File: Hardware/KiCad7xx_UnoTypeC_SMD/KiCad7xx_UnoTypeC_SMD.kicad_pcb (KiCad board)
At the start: 2 copper layers, 68.6 x 53.3 mm, 75 parts, among them J1 -, J2 -, T1 FDN340P, U1 NCP1117ST50T3G, U2 LP2985-33DBVR, U3 16U2, U4 ATMEGA328P-MU, U5 LMV358IDGKR, X1 POWERSUPPLY_DC21MMX, X2 USB-B_TH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

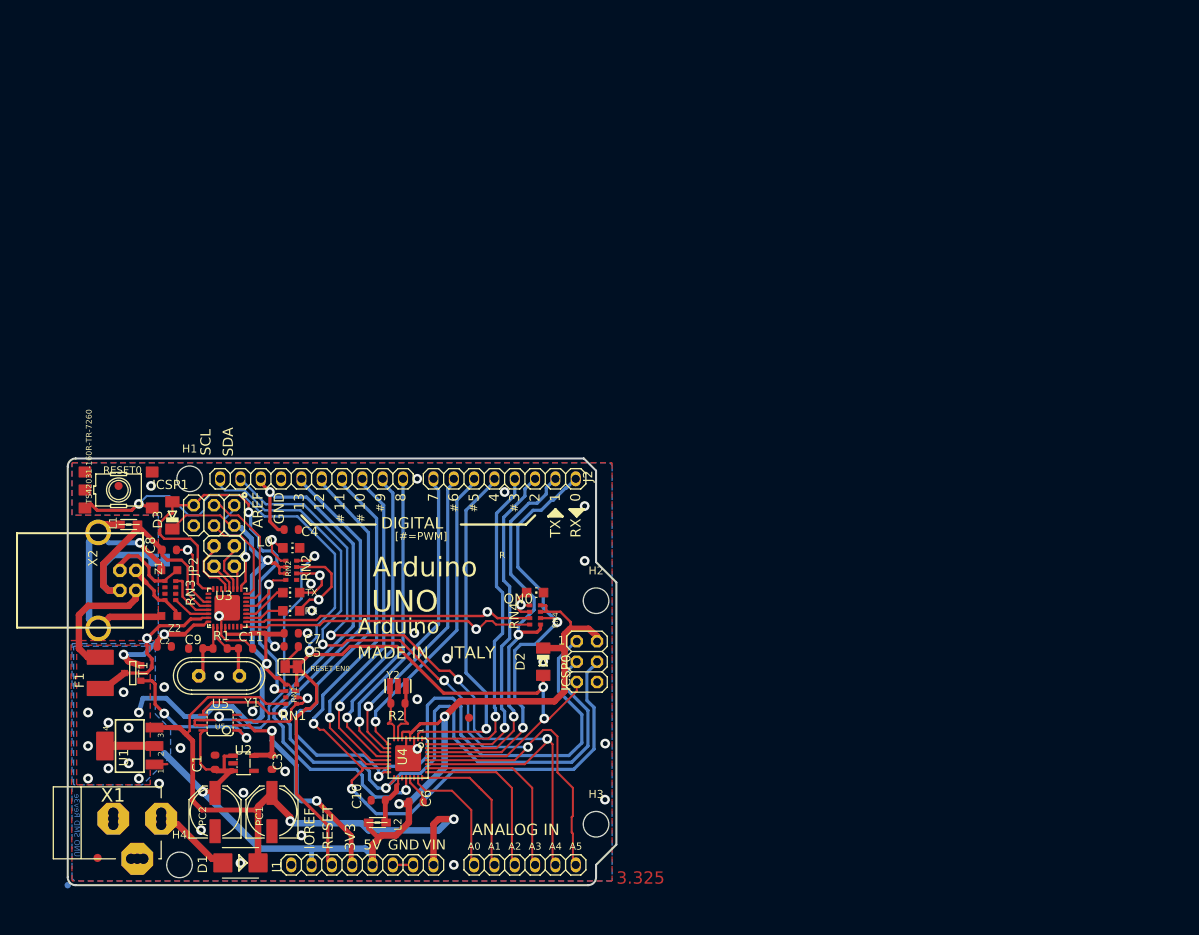
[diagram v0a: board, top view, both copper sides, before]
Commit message: feat: 変更した部品のフットプリントを再度配線
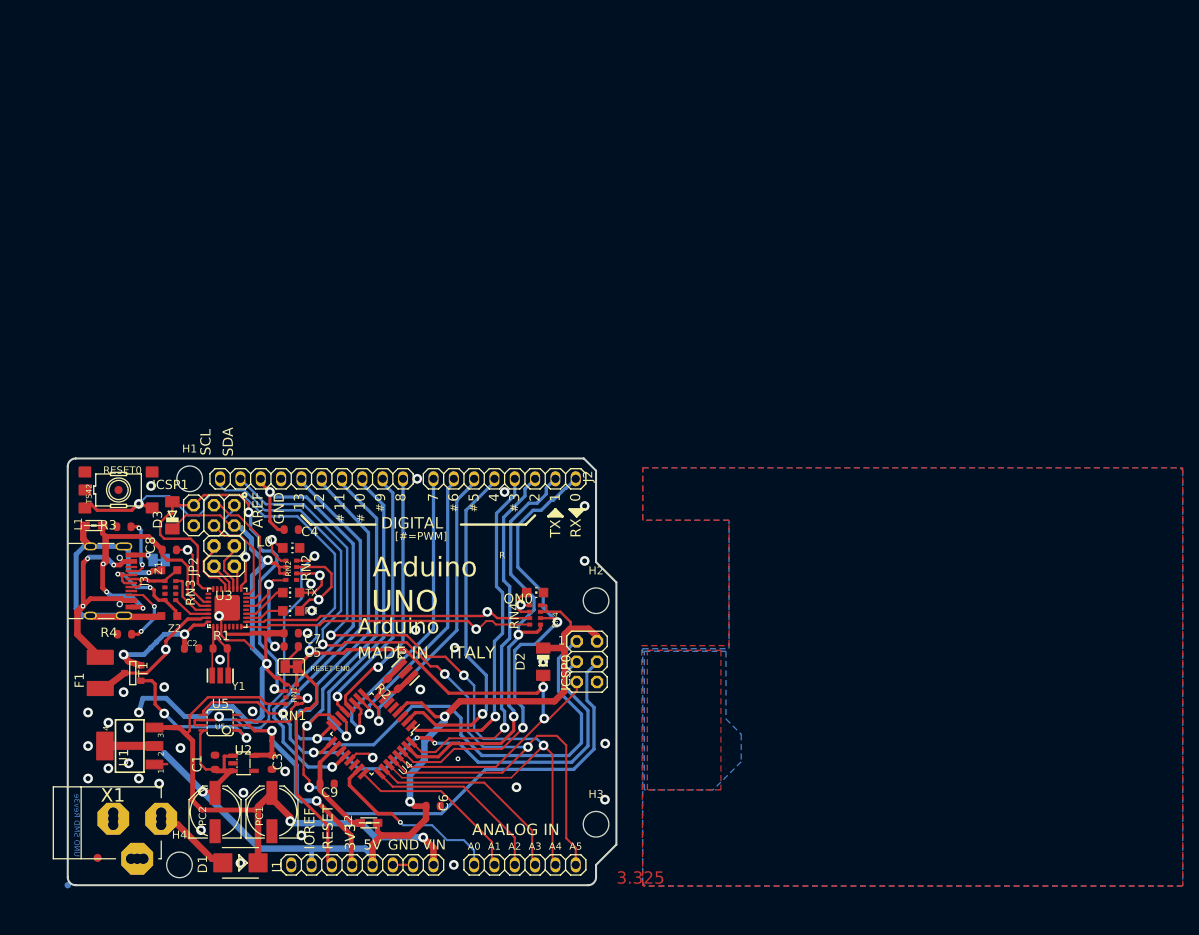
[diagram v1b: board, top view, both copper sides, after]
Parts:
- removed C10: 100nF, UNOSMD_V3:C0603-ROUND
- removed C11: 22p, UNOSMD_V3:C0603-ROUND
- removed FD2: DNP, UNOSMD_V3:FD-1-1.5
- removed TP_USH0: TP_SP, UNOSMD_V3:TP-SP
- removed X2: USB-B_TH, UNOSMD_V3:PN61729
- added J3: USB_C_Receptacle_USB2.0, Connector_USB:USB_C_Receptacle_HRO_TYPE-C-31-M-12, F.Cu at (118.1, 93.6)
- added R3: 5.1k, UNOSMD_V3:R0603-ROUND, F.Cu at (121.2, 86.9)
- added R4: 5.1k, UNOSMD_V3:R0603-ROUND, F.Cu at (121.3, 100.3)
- C9: value 22p -> 100nF
- FD1, FD3: value DNP -> FIDUCIAL-1.5MM
- GROUND0, RESET-EN0: value (none) -> SJ
- H1, H2, H3, H4: footprint UNOSMD_V3:MountingHole_3.2mm_M3_ISO14580 -> MountingHole:MountingHole_3.2mm_M3_ISO14580
- J2: value - -> PINHD-1X18
- RESET0: value TS42031-160R-TR-7260 -> TS42
- U1: value NCP1117ST50T3G -> MC33269ST
- U2: value LP2985-33DBVR -> LP2985-XXDBVR
- U3: value 16U2 -> ATMEGA16U2
- U4: value ATMEGA328P-MU -> ATmega328PB-A; footprint UNOSMD_V3:MLF32 -> Package_QFP:TQFP-32_7x7mm_P0.8mm
- U5: value LMV358IDGKR -> LMV358?MM
- X1: footprint UNOSMD_V3:POWERSUPPLY_DC-21MM -> CustomParts:POWERSUPPLY_DC-21MM
- Y1: value 16MHz -> RESONATORMU; footprint UNOSMD_V3:QS -> UNOSMD_V3:RESONATOR
- Y2: value CSTCE16M0V53-R0 16MHZ -> RESONATORMU
- Z1, Z2: value CG0603MLC-05E -> VARISTORCN0603
- moved C9 23.6 mm to (146.6, 119.0), turned to 0 degrees
- moved U4 5.48 mm to (152.2, 112.8), turned to -135 degrees
- moved L1 4.36 mm to (117.5, 86.7)
- moved C2 3.43 mm to (129.7, 102.1)
- moved TP_USBVCC0 2.73 mm to (126.5, 102.2)
- moved R2 2.54 mm to (154.9, 106.5), turned to 135 degrees
- moved C6 2.21 mm to (159.9, 121.8)
- moved Y2 2.06 mm to (156.4, 105.0), turned to -45 degrees
- moved L2 1.08 mm to (151.8, 123.9), turned to 180 degrees
- moved FD1 0.51 mm to (120.6, 82.3)
- moved Y1 0.15 mm to (133.3, 105.5)
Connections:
- net A0 renamed /A0
- net A1 renamed /A1
- net A2 renamed /A2
- net A3 renamed /A3
- net A4/SDA renamed /A4/SDA
- net A5/SCL renamed /A5/SCL
- net AREF renamed /AREF
- net CMP renamed /CMP
- net D+ renamed /D+
- net D- renamed /D-
- net DTR renamed /DTR
- net GATE_CMD renamed /GATE_CMD
- net IO0 renamed /IO0
- net IO1 renamed /IO1
- net IO2 renamed /IO2
- net IO3 renamed /IO3
- net IO4 renamed /IO4
- net IO5 renamed /IO5
- net IO6 renamed /IO6
- net IO7 renamed /IO7
- net IO8 renamed /IO8
- net IO9 renamed /IO9
- net L13 renamed /L13
- net M8RXD renamed /M8RXD
- net M8TXD renamed /M8TXD
- net MISO renamed /MISO
- net MISO2 renamed /MISO2
- net MOSI renamed /MOSI
- net MOSI2 renamed /MOSI2
- net PB4 renamed /PB4
- net PB5 renamed /PB5
- net PB6 renamed /PB6
- net PB7 renamed /PB7
- net RD+ renamed /RD+
- net RD- renamed /RD-
- net RESET renamed /PC6/RESET
- net RESET2 renamed /RESET2
- net RXLED renamed /RXLED
- net SCK renamed /SCK
- net SCK2 renamed /SCK2
- net SS renamed /SS
- net TP_VUCAP renamed /TP_VUCAP
- net TXLED renamed /TXLED
- net UGND renamed /UGND
- net USBVCC renamed /USBVCC
- net USHIELD renamed /USHIELD
- net XT2 renamed /XT2
- net XTAL1 renamed /PB6/XTAL1
- net XTAL2 renamed /PB7/XTAL2
- C9 pad 1: XT1 -> /AVCC
- D1 pad A: PWRIN -> /PWRIN
- F1 pad 2: XUSB -> /XUSB
- J1 pad 1: (no net) -> unconnected-(J1-Pad1)
- L2 pad 2: N$4 -> /AVCC
- ORIGIN0 pad X: (no net) -> unconnected-(ORIGIN0-TESTP-PadX)
- R1 pad 1: XT1 -> /XT1
- RN3 pad 2: (no net) -> unconnected-(RN3B-1-Pad2)
- RN3 pad 3: (no net) -> unconnected-(RN3C-1-Pad3)
- RN3 pad 6: (no net) -> unconnected-(RN3C-2-Pad6)
- RN3 pad 7: (no net) -> unconnected-(RN3B-2-Pad7)
- U2 pad 4: (no net) -> unconnected-(U2-NC/FB-Pad4)
- U3 pad 1: XT1 -> /XT1
- U3 pad 12: (no net) -> unconnected-(U3-(RTS/AIN5/INT6)PD6-Pad12)
- U3 pad 14: (no net) -> unconnected-(U3-(SS/PCINT0)PB0-Pad14)
- U3 pad 22: (no net) -> unconnected-(U3-(INT4/ICP1/CLK0)PC7-Pad22)
- U3 pad 23: (no net) -> unconnected-(U3-(OC1A/PCINT8)PC6-Pad23)
- U3 pad 25: (no net) -> unconnected-(U3-(PCINT9/OC1B)PC5-Pad25)
- U3 pad 26: (no net) -> unconnected-(U3-(PCINT10)PC4-Pad26)
- U3 pad 5: (no net) -> unconnected-(U3-(AIN2/PCINT11)PC2-Pad5)
- U3 pad 6: (no net) -> unconnected-(U3-(OC0B/INT0)PD0-Pad6)
- U3 pad 7: (no net) -> unconnected-(U3-(AIN0/INT1)PD1-Pad7)
- U4 pad 18: N$4 -> /AVCC
- U4 pad 19: (no net) -> unconnected-(U4-PE2-Pad19)
- U4 pad 22: (no net) -> unconnected-(U4-PE3-Pad22)
- U4 pad 3: GND -> unconnected-(U4-PE0-Pad3)
- U4 pad 6: +5V -> unconnected-(U4-PE1-Pad6)
- X1 pad 1: GND -> /PWRIN
- X1 pad 2: PWRIN -> GND
- Y1 pad 2: XT1 -> GND
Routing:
- net GND: track 61.3 -> 16.4 mm, vias 27 -> 29
- net /UGND: track 0.00 -> 38.9 mm, vias 0 -> 4
- net /XUSB: track 0.00 -> 26.7 mm, vias 0 -> 3
- net XUSB: track 16.3 -> 0.00 mm
- net /AVCC: track 0.00 -> 13.0 mm
- net /AREF: track 71.4 -> 60.3 mm
- net /SCK: track 119.6 -> 109.3 mm, vias 2 -> 4
- net PWRIN: track 10.1 -> 0.00 mm
- net /PWRIN: track 0.00 -> 10.1 mm
- net /IO9: track 42.5 -> 33.2 mm
- net Net-(J3-CC2): track 0.00 -> 8.62 mm, vias 0 -> 2
- net /IO8: track 40.6 -> 32.1 mm
- net /A0: track 15.7 -> 24.0 mm, vias 0 -> 1
- net /MISO: track 107.1 -> 98.9 mm
- net XT1: track 8.01 -> 0.00 mm
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
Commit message: feat: 電源回路を見直しダイオードSS54B(FOSAN)の追加
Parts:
- added D4: SS54B (FOSAN), Diode_SMD:D_SMB, F.Cu at (161.2, 122.5)
- added FD2: FIDUCIAL-1.5MM, UNOSMD_V3:FD-1-1.5, F.Cu at (126.8, 23.5)
- D1: value M7 -> SS54B (FOSAN); footprint UNOSMD_V3:SMB -> Diode_SMD:D_SMB
- U5: value LMV358?MM -> LMV358IDGKR
- moved C6 5.55 mm to (154.4, 121.5), turned to 0 degrees
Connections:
- J1 pad 8: VIN -> /VIN
- PC1 pad +: VIN -> VCC
- RN1 pad 8: VIN -> VCC
- U1 pad 3: VIN -> VCC
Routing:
- net VIN: track 74.6 -> 0.00 mm, vias 2 -> 0
- net VCC: track 0.00 -> 73.7 mm, vias 0 -> 2
- net /VIN: track 0.00 -> 8.27 mm
- net /A1: track 22.6 -> 24.9 mm
- net +5V: track 228.4 -> 226.1 mm
- net /A2: track 23.6 -> 24.6 mm
- net /A0: track 24.0 -> 24.9 mm

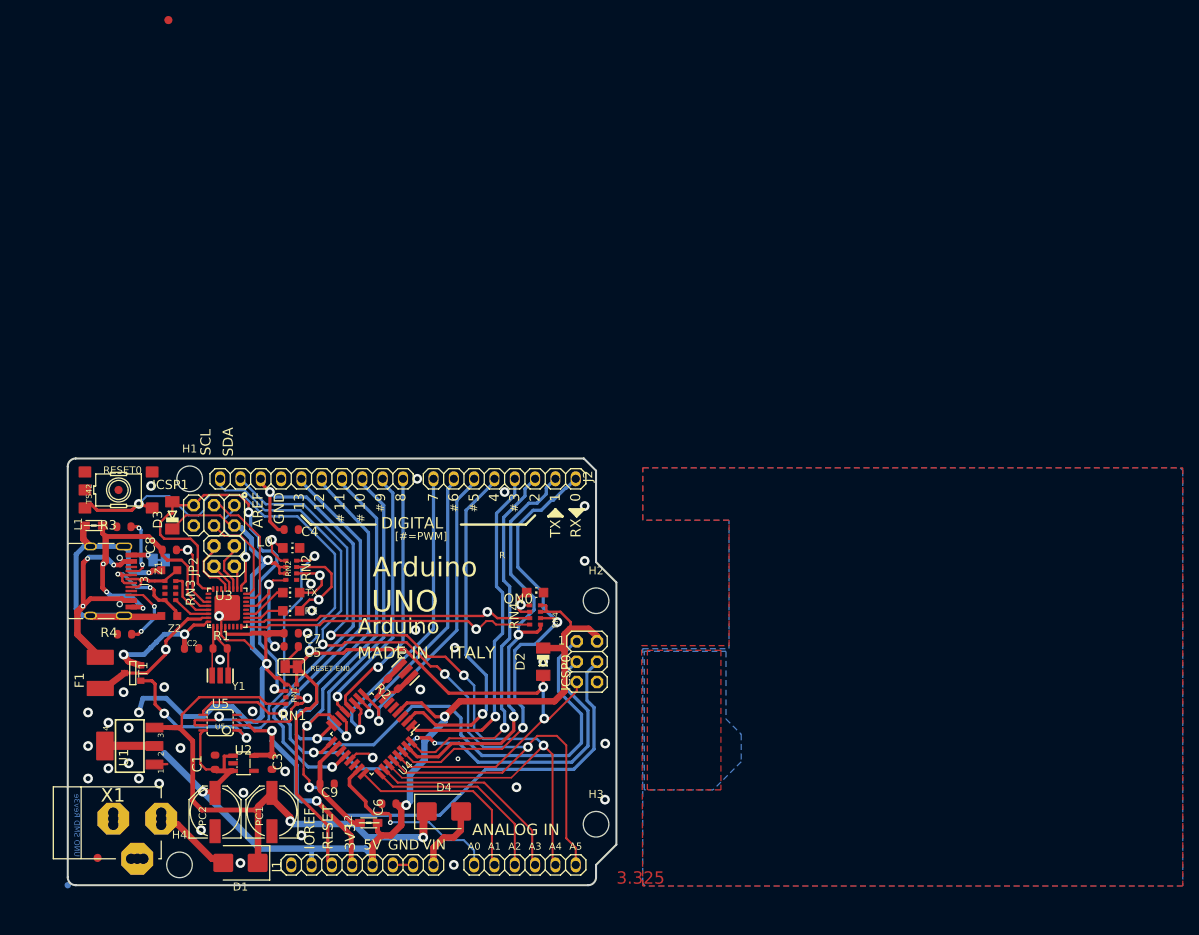
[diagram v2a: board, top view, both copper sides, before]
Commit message: feat: UnoTypeC_SMD Rev1Cのガーバファイルを作成
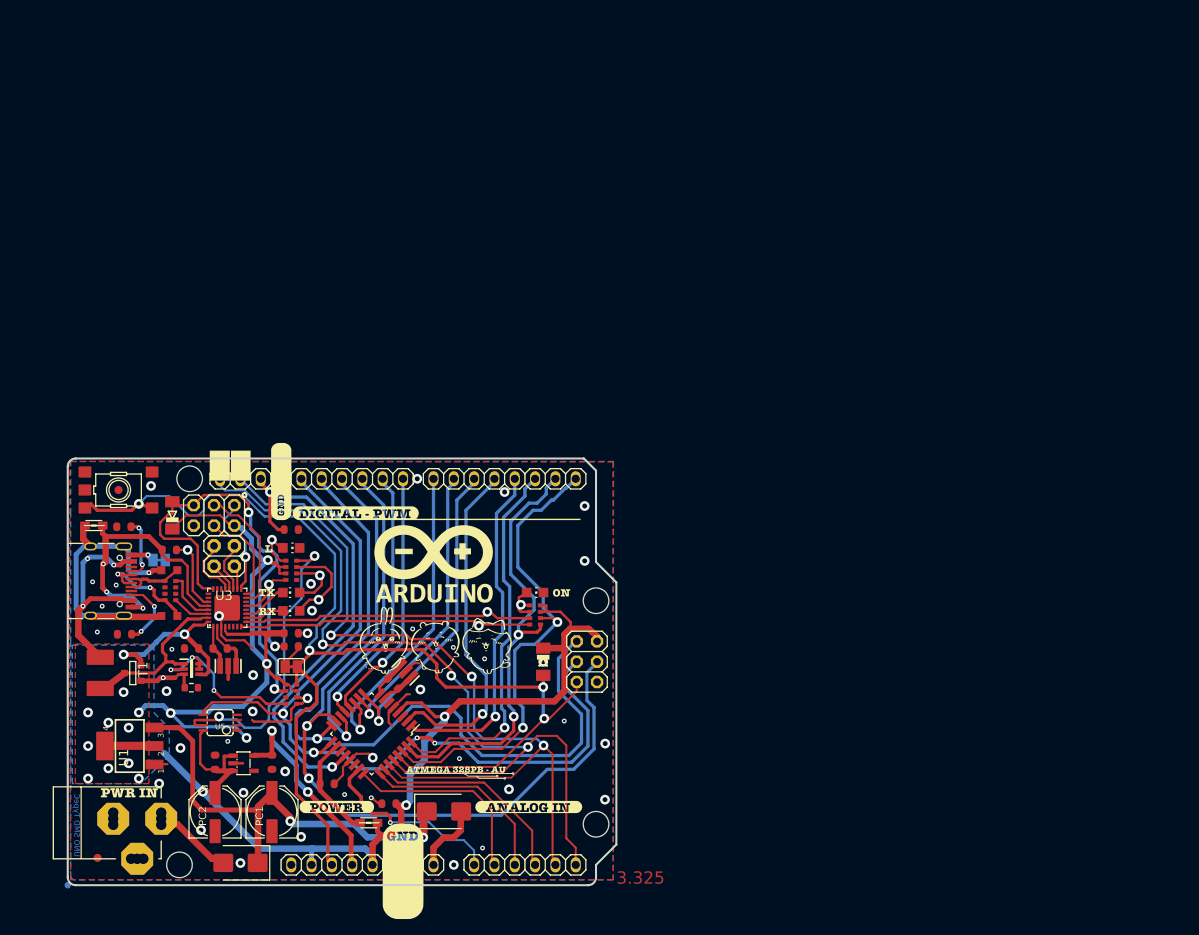
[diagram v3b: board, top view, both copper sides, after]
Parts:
- removed FD2: FIDUCIAL-1.5MM, UNOSMD_V3:FD-1-1.5
- removed TP_CMP0, TP_GATE0, TP_USBVCC0: TP_SP, UNOSMD_V3:TP-SP
- added G***: LOGO, footprint:シルク_Front_Rev1c_59-5, F.Cu at (148.4, 106.1)
- added G***: LOGO, footprint:シルク_Back_Rev1b_58, B.Cu at (148.4, 105.6)
- added R5: 47K, Resistor_SMD:R_0603_1608Metric, F.Cu at (129.7, 107.0)
- added U6: BCM857BS, Nexperia_TRANSISTOR_BCM857BS_SOT-363_Component:SOT65P210X110-6N, F.Cu at (129.7, 104.6)
- F1: value MF-MSMF050-2 500mA -> MF-MSMF110/16-2A
- T1: value FDN340P -> PMOS/FDN340P(onsemi)/2A
- moved Y1 1.55 mm to (134.3, 104.3)
- moved TP_TX0 0.55 mm to (165.6, 99.2)
- turned C2 to 0 degrees
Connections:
- C3 pad 2: +3V3 -> +3.3V
- J1 pad 4: +3V3 -> +3.3V
- RN1 pad 1: /CMP -> GND
- RN1 pad 2: /CMP -> (no net)
- RN1 pad 7: GND -> (no net)
- RN1 pad 8: VCC -> Net-(RN1A-2)
- T1 pad 3: /GATE_CMD -> Net-(T1-G)
- U2 pad 5: +3V3 -> +3.3V
- U5 pad 1: /GATE_CMD -> unconnected-(U5-Pad1)
- U5 pad 2: +3V3 -> unconnected-(U5-Pad2)
- U5 pad 3: /CMP -> unconnected-(U5-Pad3)
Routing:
- net +3V3: track 32.0 -> 0.00 mm, vias 2 -> 0
- net GND: track 16.4 -> 43.1 mm, vias 29 -> 41
- net +3.3V: track 0.00 -> 26.3 mm, vias 0 -> 2
- net Net-(RN1A-2): track 0.00 -> 22.9 mm, vias 0 -> 3
- net /GATE_CMD: track 19.2 -> 0.00 mm, vias 2 -> 0
- net VCC: track 73.7 -> 57.7 mm
- net /CMP: track 12.3 -> 0.00 mm, vias 1 -> 0
- net +5V: track 226.1 -> 237.2 mm, vias 17 -> 19
- net Net-(T1-G): track 0.00 -> 7.41 mm, vias 0 -> 1
- net /USBVCC: track 19.2 -> 22.5 mm, vias 1 -> 0
- net /XT1: track 6.50 -> 5.70 mm
- net /A5/SCL: track 106.1 -> 106.9 mm
- net /M8TXD: track 37.4 -> 36.7 mm
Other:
- board text added: "UNO SMD TypeC"
- board text removed: "#"
- board text removed: "0"
- board text removed: "1"
- board text removed: "10"
- board text removed: "11"
- board text removed: "12"
- board text removed: "13"
- board text removed: "2"
- board text removed: "3"
- board text removed: "3V3"
- board text removed: "4"
- board text removed: "5"
- board text removed: "5V"
- board text removed: "6"
- board text removed: "7"
- board text removed: "8"
- board text removed: "9"
- board text removed: "A0"
- board text removed: "A1"
- board text removed: "A2"
- board text removed: "A3"
- board text removed: "A4"
- board text removed: "A5"
- board text removed: "ANALOG IN"
- board text removed: "AREF"
- board text removed: "Arduino"
- board text removed: "DIGITAL"
- board text removed: "GND"
- board text removed: "IOREF"
- board text removed: "ITALY"
- board text removed: "MADE IN"
- board text removed: "R"
- board text removed: "RESET"
- board text removed: "RN1"
- board text removed: "RN2"
- board text removed: "RN4"
- board text removed: "SCL"
- board text removed: "SDA"
- board text removed: "U5"
- board text removed: "UNO"
- board text removed: "UNO SMD Rev3e"
- board text removed: "VIN"
- board text removed: "[#=PWM]"
- board text removed: "designed by"
- board text removed: "tinker it"
